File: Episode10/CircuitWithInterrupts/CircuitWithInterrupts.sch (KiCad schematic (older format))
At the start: 0 parts

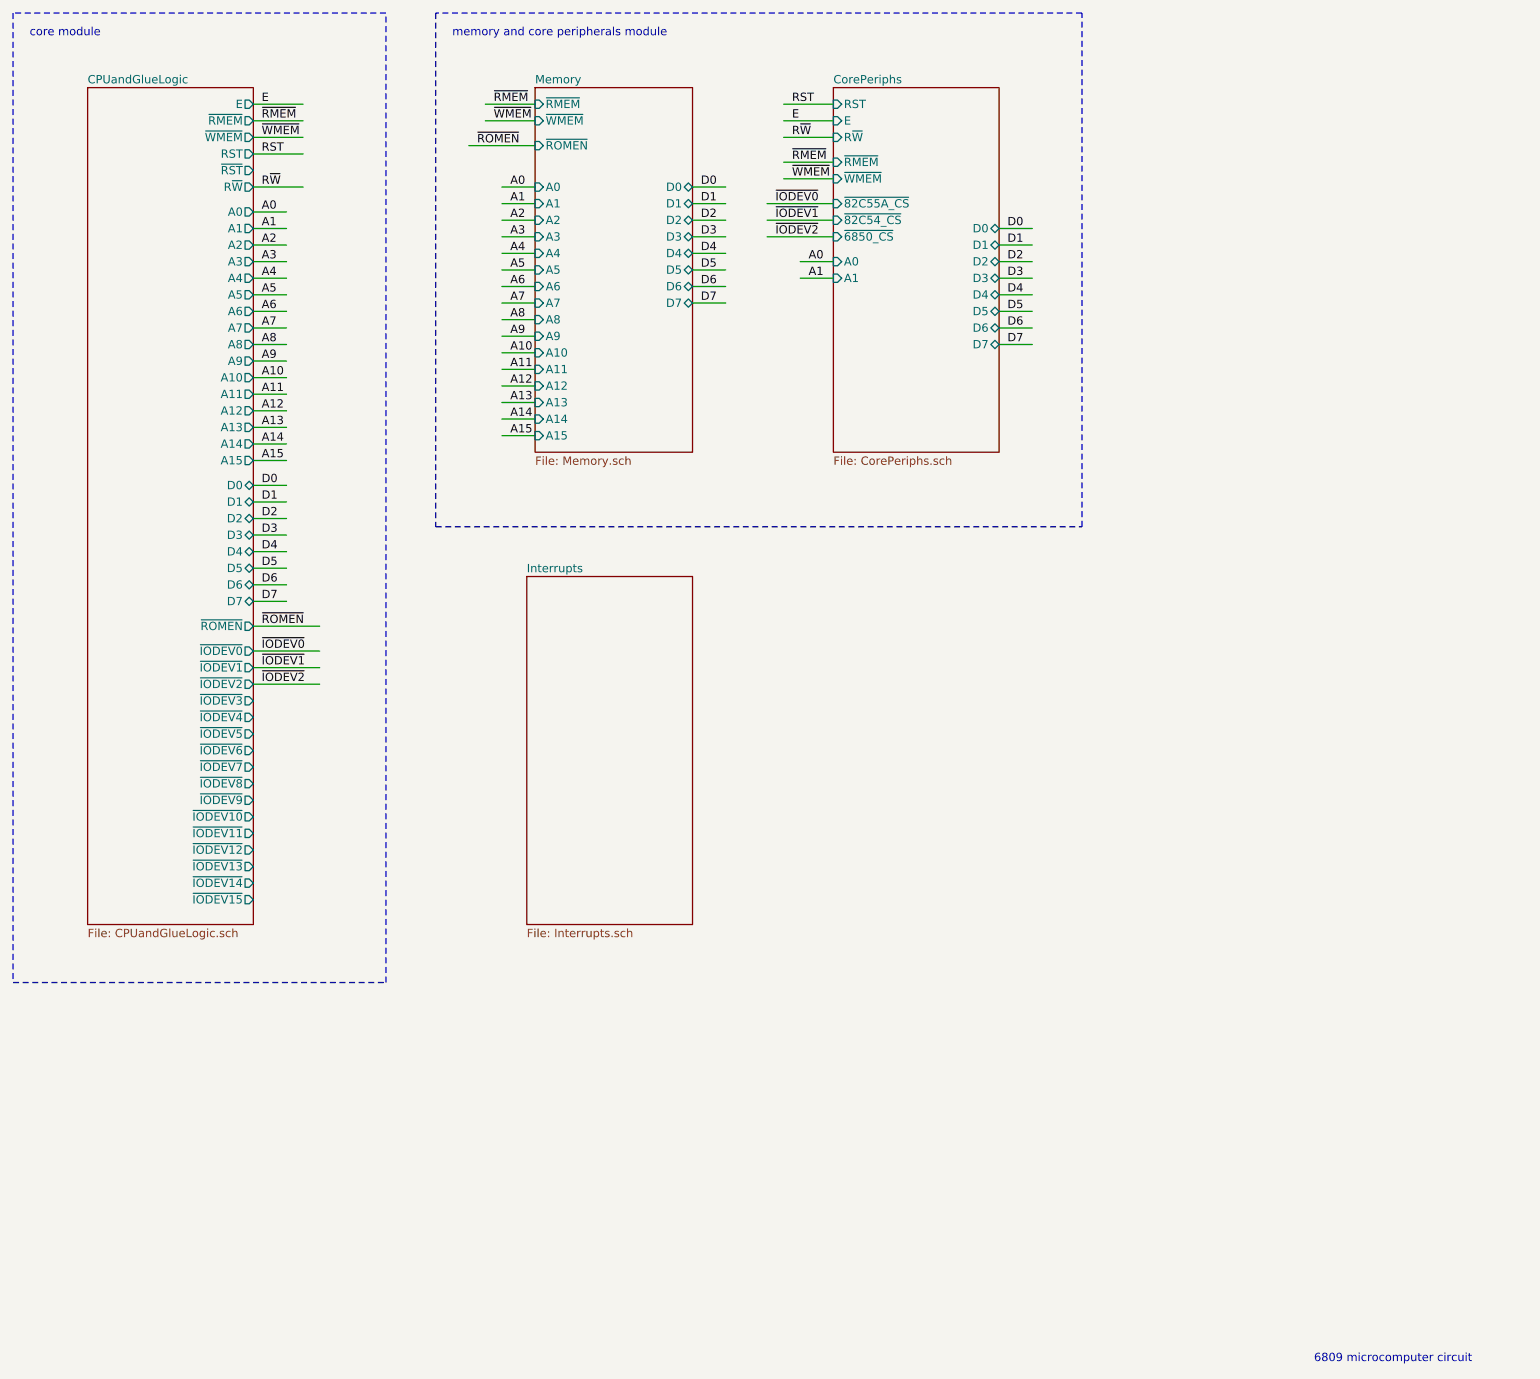
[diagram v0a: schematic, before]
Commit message: integrated interrupt controller
Added ~IRQ input to core module, and changed the
wiring of the CPU's ~IRQ input to feed in the ~IRQ
output of the interrupt controller.  (A pull-up
resistor will keep this input high when the interrupt
controller isn't installed.)

Have the peripheral module send the Timer 1 output
to the interrupt controller's ~IRQ3 input.  This will
be the system periodic timer interrupt.

Also have the peripheral module export the pins of
Port C, and use PC0 and PC1 to clear the flip flops
that latch a pulse on ~IRQ3 and ~IRQ6, which are
edge-triggered.
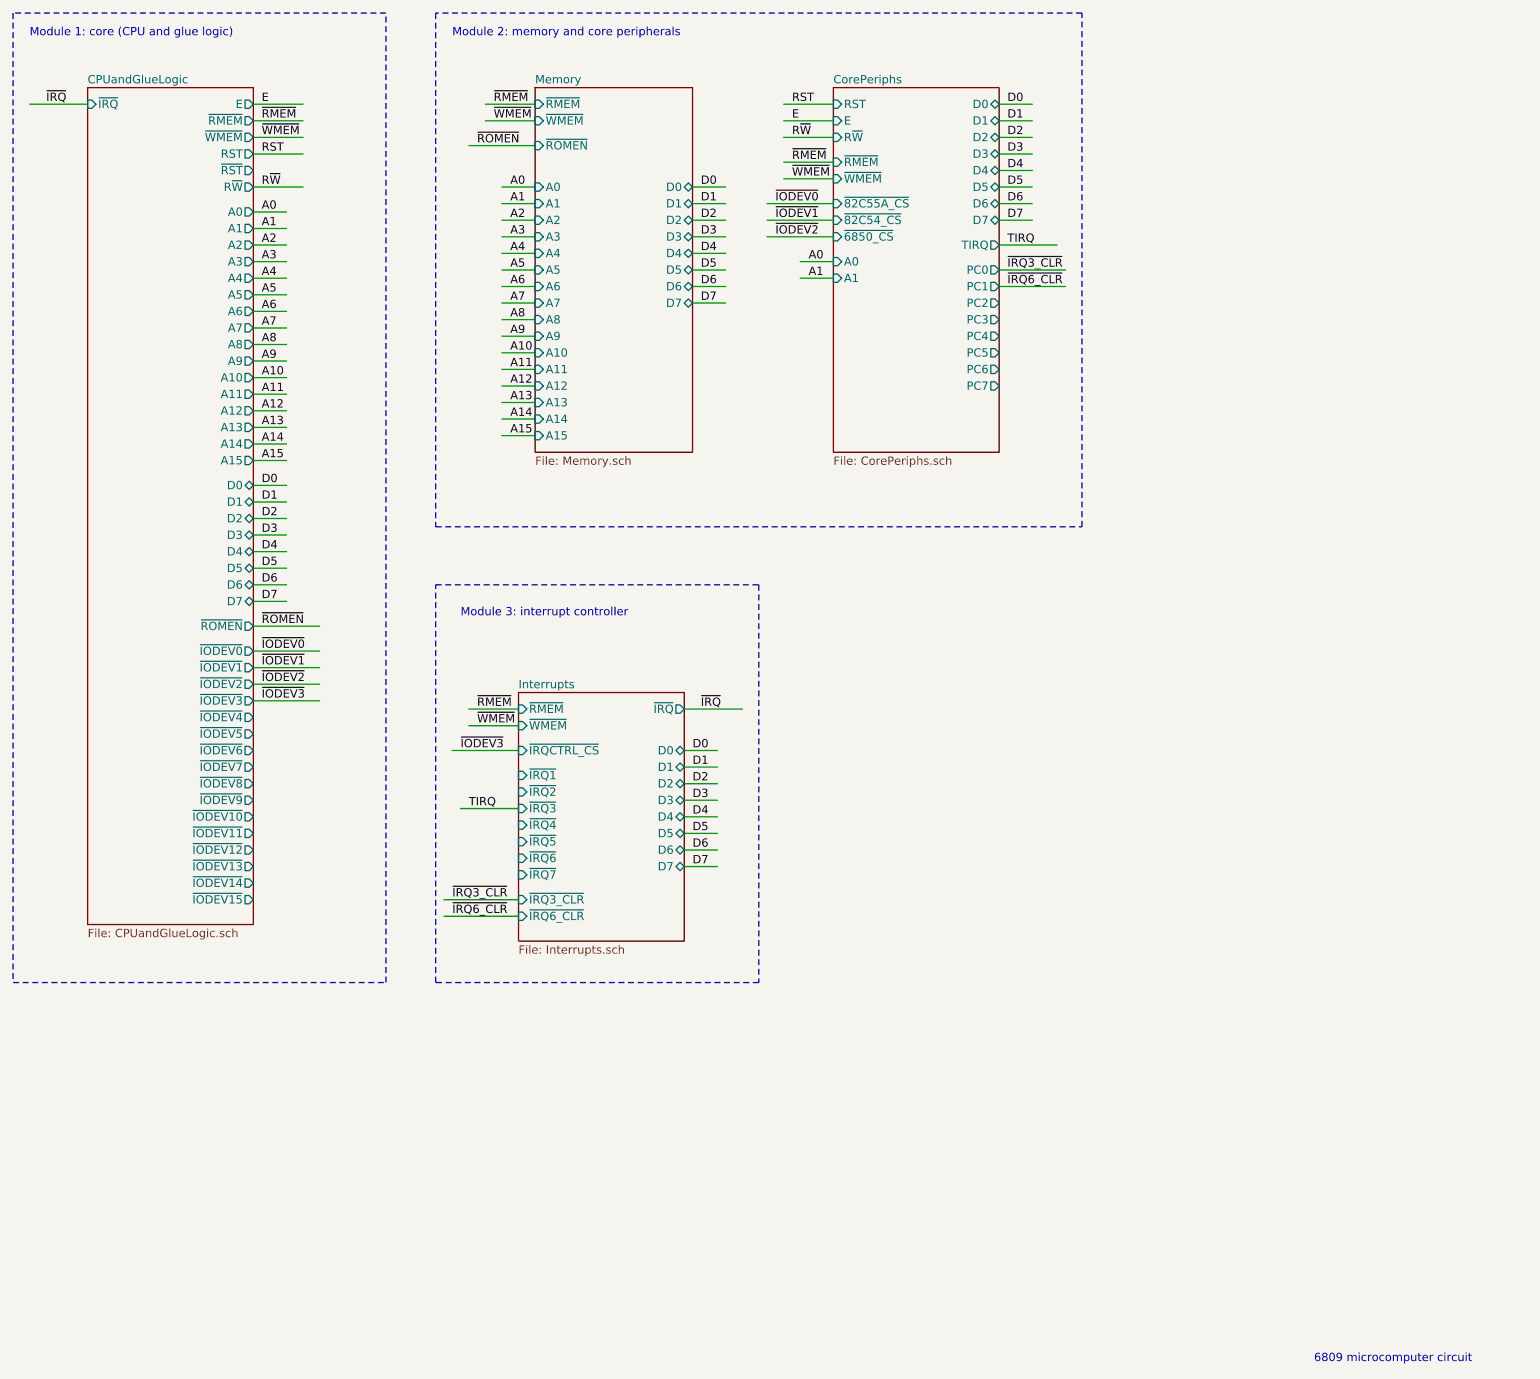
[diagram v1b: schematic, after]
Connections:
- net labels added: TIRQ, ~IODEV3, ~IRQ, ~IRQ3_CLR, ~IRQ6_CLR
- wire segments 78 -> 98
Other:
- note added: "Module 1: core (CPU and glue logic)"
- note added: "Module 2: memory and core peripherals"
- note added: "Module 3: interrupt controller"
- note removed: "core module"
- note removed: "memory and core peripherals module"
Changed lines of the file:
@@
 F47 "~ROMEN~" O R 3200 4950 50
 F48 "R~W" O R 3200 2300 50
+F49 "~IRQ" I L 2200 1800 50
 $EndSheet
 $Sheet
@@
 F6 "A0" I L 6700 2750 50
 F7 "A1" I L 6700 2850 50
-F8 "D0" B R 7700 2550 50
-F9 "D1" B R 7700 2650 50
-F10 "D2" B R 7700 2750 50
-F11 "D3" B R 7700 2850 50
-F12 "D4" B R 7700 2950 50
-F13 "D5" B R 7700 3050 50
-F14 "D6" B R 7700 3150 50
-F15 "D7" B R 7700 3250 50
+F8 "D0" B R 7700 1800 50
+F9 "D1" B R 7700 1900 50
+F10 "D2" B R 7700 2000 50
+F11 "D3" B R 7700 2100 50
+F12 "D4" B R 7700 2200 50
+F13 "D5" B R 7700 2300 50
+F14 "D6" B R 7700 2400 50
+F15 "D7" B R 7700 2500 50
 F16 "~82C54_CS" I L 6700 2500 50
 F17 "E" I L 6700 1900 50
 F18 "R~W" I L 6700 2000 50
 F19 "~6850_CS" I L 6700 2600 50
+F20 "TIRQ" O R 7700 2650 50
+F21 "PC0" O R 7700 2800 50
+F22 "PC1" O R 7700 2900 50
+F23 "PC2" O R 7700 3000 50
+F24 "PC3" O R 7700 3100 50
+F25 "PC4" O R 7700 3200 50
+F26 "PC5" O R 7700 3300 50
+F27 "PC6" O R 7700 3400 50
+F28 "PC7" O R 7700 3500 50
 $EndSheet
 Wire Wire Line
@@
 A1
 Wire Wire Line
-	7700 2550 7900 2550
-Wire Wire Line
-	7700 2650 7900 2650
-Wire Wire Line
-	7700 2750 7900 2750
-Wire Wire Line
-	7700 2850 7900 2850
-Wire Wire Line
-	7700 2950 7900 2950
-Wire Wire Line
-	7700 3050 7900 3050
-Wire Wire Line
-	7700 3150 7900 3150
-Wire Wire Line
-	7700 3250 7900 3250
-Text Label 7750 2550 0    50   ~ 0
+	7700 1800 7900 1800
+Wire Wire Line
+	7700 1900 7900 1900
+Wire Wire Line
+	7700 2000 7900 2000
+Wire Wire Line
+	7700 2100 7900 2100
+Wire Wire Line
+	7700 2200 7900 2200
+Wire Wire Line
+	7700 2300 7900 2300
+Wire Wire Line
+	7700 2400 7900 2400
+Wire Wire Line
+	7700 2500 7900 2500
+Text Label 7750 1800 0    50   ~ 0
 D0
-Text Label 7750 2650 0    50   ~ 0
+Text Label 7750 1900 0    50   ~ 0
 D1
-Text Label 7750 2750 0    50   ~ 0
+Text Label 7750 2000 0    50   ~ 0
 D2
-Text Label 7750 2850 0    50   ~ 0
+Text Label 7750 2100 0    50   ~ 0
 D3
-Text Label 7750 2950 0    50   ~ 0
+Text Label 7750 2200 0    50   ~ 0
 D4
-Text Label 7750 3050 0    50   ~ 0
+Text Label 7750 2300 0    50   ~ 0
 D5
-Text Label 7750 3150 0    50   ~ 0
+Text Label 7750 2400 0    50   ~ 0
 D6
-Text Label 7750 3250 0    50   ~ 0
+Text Label 7750 2500 0    50   ~ 0
 D7
 Wire Wire Line
@@
 	4000 1250 1750 1250
 Text Notes 1850 1400 0    50   ~ 0
-core module
+Module 1: core (CPU and glue logic)
 Wire Notes Line
 	4300 1250 4300 4350
@@
 	8200 1250 4300 1250
 Text Notes 4400 1400 0    50   ~ 0
-memory and core peripherals module
+Module 2: memory and core peripherals
 $Sheet
-S 4850 4650 1000 2100
+S 4800 5350 1000 1500
 U 5E12A5CF
 F0 "Interrupts" 50
 F1 "Interrupts.sch" 50
+F2 "~IRQ1" I L 4800 5850 50
+F3 "~IRQ2" I L 4800 5950 50
+F4 "~IRQ4" I L 4800 6150 50
+F5 "~IRQ5" I L 4800 6250 50
+F6 "~IRQ7" I L 4800 6450 50
+F7 "~IRQ3" I L 4800 6050 50
+F8 "~IRQ6" I L 4800 6350 50
+F9 "~IRQ" O R 5800 5450 50
+F10 "~RMEM" I L 4800 5450 50
+F11 "~IRQCTRL_CS" I L 4800 5700 50
+F12 "~IRQ3_CLR" I L 4800 6600 50
+F13 "~IRQ6_CLR" I L 4800 6700 50
+F14 "D0" B R 5800 5700 50
+F15 "D1" B R 5800 5800 50
+F16 "D2" B R 5800 5900 50
+F17 "D3" B R 5800 6000 50
+F18 "D4" B R 5800 6100 50
+F19 "D5" B R 5800 6200 50
+F20 "D6" B R 5800 6300 50
+F21 "D7" B R 5800 6400 50
+F22 "~WMEM" I L 4800 5550 50
 $EndSheet
+Wire Notes Line
+	4300 4700 6250 4700
+Wire Notes Line
+	6250 4700 6250 7100
+Wire Notes Line
+	6250 7100 4300 7100
+Wire Notes Line
+	4300 7100 4300 4700
+Text Notes 4450 4900 0    50   ~ 0
+Module 3: interrupt controller
+Wire Wire Line
+	5800 5700 6000 5700
+Wire Wire Line
+	5800 5800 6000 5800
+Wire Wire Line
+	5800 5900 6000 5900
+Wire Wire Line
+	5800 6000 6000 6000
+Wire Wire Line
+	5800 6100 6000 6100
+Wire Wire Line
+	5800 6200 6000 6200
+Wire Wire Line
+	5800 6300 6000 6300
+Wire Wire Line
+	5800 6400 6000 6400
+Text Label 5850 5700 0    50   ~ 0
+D0
+Text Label 5850 5800 0    50   ~ 0
+D1
+Text Label 5850 5900 0    50   ~ 0
+D2
+Text Label 5850 6000 0    50   ~ 0
+D3
+Text Label 5850 6100 0    50   ~ 0
+D4
+Text Label 5850 6200 0    50   ~ 0
+D5
+Text Label 5850 6300 0    50   ~ 0
+D6
+Text Label 5850 6400 0    50   ~ 0
+D7
+Wire Wire Line
+	4500 5450 4800 5450
+Wire Wire Line
+	4500 5550 4800 5550
+Text Label 4550 5450 0    50   ~ 0
+~RMEM~
+Text Label 4550 5550 0    50   ~ 0
+~WMEM~
+Wire Wire Line
+	3200 5400 3600 5400
+Text Label 3250 5400 0    50   ~ 0
+~IODEV3
+Wire Wire Line
+	4400 5700 4800 5700
+Text Label 4450 5700 0    50   ~ 0
+~IODEV3
+Wire Wire Line
+	2200 1800 1850 1800
+Text Label 1950 1800 0    50   ~ 0
+~IRQ
+Wire Wire Line
+	6150 5450 5800 5450
+Text Label 5900 5450 0    50   ~ 0
+~IRQ
+Wire Wire Line
+	7700 2650 8050 2650
+Text Label 7750 2650 0    50   ~ 0
+TIRQ
+Wire Wire Line
+	4450 6050 4800 6050
+Text Label 4500 6050 0    50   ~ 0
+TIRQ
+Wire Wire Line
+	7700 2800 8100 2800
+Wire Wire Line
+	7700 2900 8100 2900
+Text Label 7750 2800 0    50   ~ 0
+~IRQ3_CLR
+Text Label 7750 2900 0    50   ~ 0
+~IRQ6_CLR
+Wire Wire Line
+	4350 6600 4800 6600
+Wire Wire Line
+	4350 6700 4800 6700
+Text Label 4400 6600 0    50   ~ 0
+~IRQ3_CLR
+Text Label 4400 6700 0    50   ~ 0
+~IRQ6_CLR
 $EndSCHEMATC
